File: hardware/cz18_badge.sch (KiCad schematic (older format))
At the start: 18 parts, among them U1 NRF24L01_Breakout

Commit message: Added 433MHz modules
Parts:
- RF1: footprint (none) -> Sensors:RF_Receiver_433_MHz
- RF2: footprint (none) -> Sensors:RF_Transmitter_433_MHz
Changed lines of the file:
@@
 LIBS:Zilog
 LIBS:skoro_sensors
-LIBS:cz18_badge-cache
 EELAYER 25 0
 EELAYER END
@@
 VCC
 $Comp
-L GNDREF #PWR2
+L GNDREF #PWR01
 U 1 1 5B016875
 P 1100 1400
-F 0 "#PWR2" H 1100 1150 50  0001 C CNN
+F 0 "#PWR01" H 1100 1150 50  0001 C CNN
 F 1 "GNDREF" H 1100 1250 50  0000 C CNN
 F 2 "" H 1100 1400 50  0001 C CNN
@@
 $EndComp
 $Comp
-L GNDREF #PWR6
+L GNDREF #PWR02
 U 1 1 5B016893
 P 2000 1400
-F 0 "#PWR6" H 2000 1150 50  0001 C CNN
+F 0 "#PWR02" H 2000 1150 50  0001 C CNN
 F 1 "GNDREF" H 2000 1250 50  0000 C CNN
 F 2 "" H 2000 1400 50  0001 C CNN
@@
 $EndComp
 $Comp
-L GNDREF #PWR8
+L GNDREF #PWR03
 U 1 1 5B016988
 P 2900 1400
-F 0 "#PWR8" H 2900 1150 50  0001 C CNN
+F 0 "#PWR03" H 2900 1150 50  0001 C CNN
 F 1 "GNDREF" H 2900 1250 50  0000 C CNN
 F 2 "" H 2900 1400 50  0001 C CNN
@@
 $EndComp
 $Comp
-L GNDREF #PWR10
+L GNDREF #PWR04
 U 1 1 5B016A28
 P 3800 1400
-F 0 "#PWR10" H 3800 1150 50  0001 C CNN
+F 0 "#PWR04" H 3800 1150 50  0001 C CNN
 F 1 "GNDREF" H 3800 1250 50  0000 C CNN
 F 2 "" H 3800 1400 50  0001 C CNN
@@
 $EndComp
 $Comp
-L GNDREF #PWR12
+L GNDREF #PWR05
 U 1 1 5B016A4B
 P 4750 1400
-F 0 "#PWR12" H 4750 1150 50  0001 C CNN
+F 0 "#PWR05" H 4750 1150 50  0001 C CNN
 F 1 "GNDREF" H 4750 1250 50  0000 C CNN
 F 2 "" H 4750 1400 50  0001 C CNN
@@
 $EndComp
 $Comp
-L GNDREF #PWR5
+L GNDREF #PWR06
 U 1 1 5B0170CF
 P 1600 750
-F 0 "#PWR5" H 1600 500 50  0001 C CNN
+F 0 "#PWR06" H 1600 500 50  0001 C CNN
 F 1 "GNDREF" H 1600 600 50  0000 C CNN
 F 2 "" H 1600 750 50  0001 C CNN
@@
 $EndComp
 $Comp
-L GNDREF #PWR1
+L GNDREF #PWR07
 U 1 1 5B0175AF
 P 700 750
-F 0 "#PWR1" H 700 500 50  0001 C CNN
+F 0 "#PWR07" H 700 500 50  0001 C CNN
 F 1 "GNDREF" H 700 600 50  0000 C CNN
 F 2 "" H 700 750 50  0001 C CNN
@@
 $EndComp
 $Comp
-L GNDREF #PWR7
+L GNDREF #PWR08
 U 1 1 5B0179B3
 P 2500 750
-F 0 "#PWR7" H 2500 500 50  0001 C CNN
+F 0 "#PWR08" H 2500 500 50  0001 C CNN
 F 1 "GNDREF" H 2500 600 50  0000 C CNN
 F 2 "" H 2500 750 50  0001 C CNN
@@
 $EndComp
 $Comp
-L GNDREF #PWR9
+L GNDREF #PWR09
 U 1 1 5B017A92
 P 3400 750
-F 0 "#PWR9" H 3400 500 50  0001 C CNN
+F 0 "#PWR09" H 3400 500 50  0001 C CNN
 F 1 "GNDREF" H 3400 600 50  0000 C CNN
 F 2 "" H 3400 750 50  0001 C CNN
@@
 $EndComp
 $Comp
-L GNDREF #PWR11
+L GNDREF #PWR010
 U 1 1 5B017AE5
 P 4350 750
-F 0 "#PWR11" H 4350 500 50  0001 C CNN
+F 0 "#PWR010" H 4350 500 50  0001 C CNN
 F 1 "GNDREF" H 4350 600 50  0000 C CNN
 F 2 "" H 4350 750 50  0001 C CNN
@@
 $EndComp
 $Comp
-L GNDREF #PWR14
+L GNDREF #PWR011
 U 1 1 5B01D44A
 P 9450 6150
-F 0 "#PWR14" H 9450 5900 50  0001 C CNN
+F 0 "#PWR011" H 9450 5900 50  0001 C CNN
 F 1 "GNDREF" H 9450 6000 50  0000 C CNN
 F 2 "" H 9450 6150 50  0001 C CNN
@@
 $EndComp
 $Comp
-L GNDREF #PWR3
+L GNDREF #PWR012
 U 1 1 5B01DF4E
 P 1250 6250
-F 0 "#PWR3" H 1250 6000 50  0001 C CNN
+F 0 "#PWR012" H 1250 6000 50  0001 C CNN
 F 1 "GNDREF" H 1250 6100 50  0000 C CNN
 F 2 "" H 1250 6250 50  0001 C CNN
@@
 $EndComp
 $Comp
-L GNDREF #PWR4
+L GNDREF #PWR013
 U 1 1 5B01DFBD
 P 1250 6700
-F 0 "#PWR4" H 1250 6450 50  0001 C CNN
+F 0 "#PWR013" H 1250 6450 50  0001 C CNN
 F 1 "GNDREF" H 1250 6550 50  0000 C CNN
 F 2 "" H 1250 6700 50  0001 C CNN
@@
 Connection ~ 9450 3650
 $Comp
-L VCC #PWR15
+L VCC #PWR014
 U 1 1 5B01FFB2
 P 9500 3550
-F 0 "#PWR15" H 9500 3400 50  0001 C CNN
+F 0 "#PWR014" H 9500 3400 50  0001 C CNN
 F 1 "VCC" H 9500 3700 50  0000 C CNN
 F 2 "" H 9500 3550 50  0001 C CNN
@@
 $EndComp
 $Comp
-L GNDREF #PWR13
+L GNDREF #PWR015
 U 1 1 5B024896
 P 5950 7400
-F 0 "#PWR13" H 5950 7150 50  0001 C CNN
+F 0 "#PWR015" H 5950 7150 50  0001 C CNN
 F 1 "GNDREF" H 5950 7250 50  0000 C CNN
 F 2 "" H 5950 7400 50  0001 C CNN
@@
 F 0 "RF1" H 3850 6950 60  0000 C CNN
 F 1 "RF_Receiver_433_MHz" H 3850 6850 60  0000 C CNN
-F 2 "" H 3950 6300 60  0000 C CNN
+F 2 "Sensors:RF_Receiver_433_MHz" H 3950 6300 60  0001 C CNN
 F 3 "" H 3950 6300 60  0000 C CNN
 	1    3850 6300
@@
 F 0 "RF2" H 3850 7950 60  0000 C CNN
 F 1 "RF_Transmitter_433_MHz" H 3850 7850 60  0000 C CNN
-F 2 "" H 3850 7150 60  0000 C CNN
+F 2 "Sensors:RF_Transmitter_433_MHz" H 3850 7150 60  0001 C CNN
 F 3 "" H 3850 7150 60  0000 C CNN
 	1    3850 7150

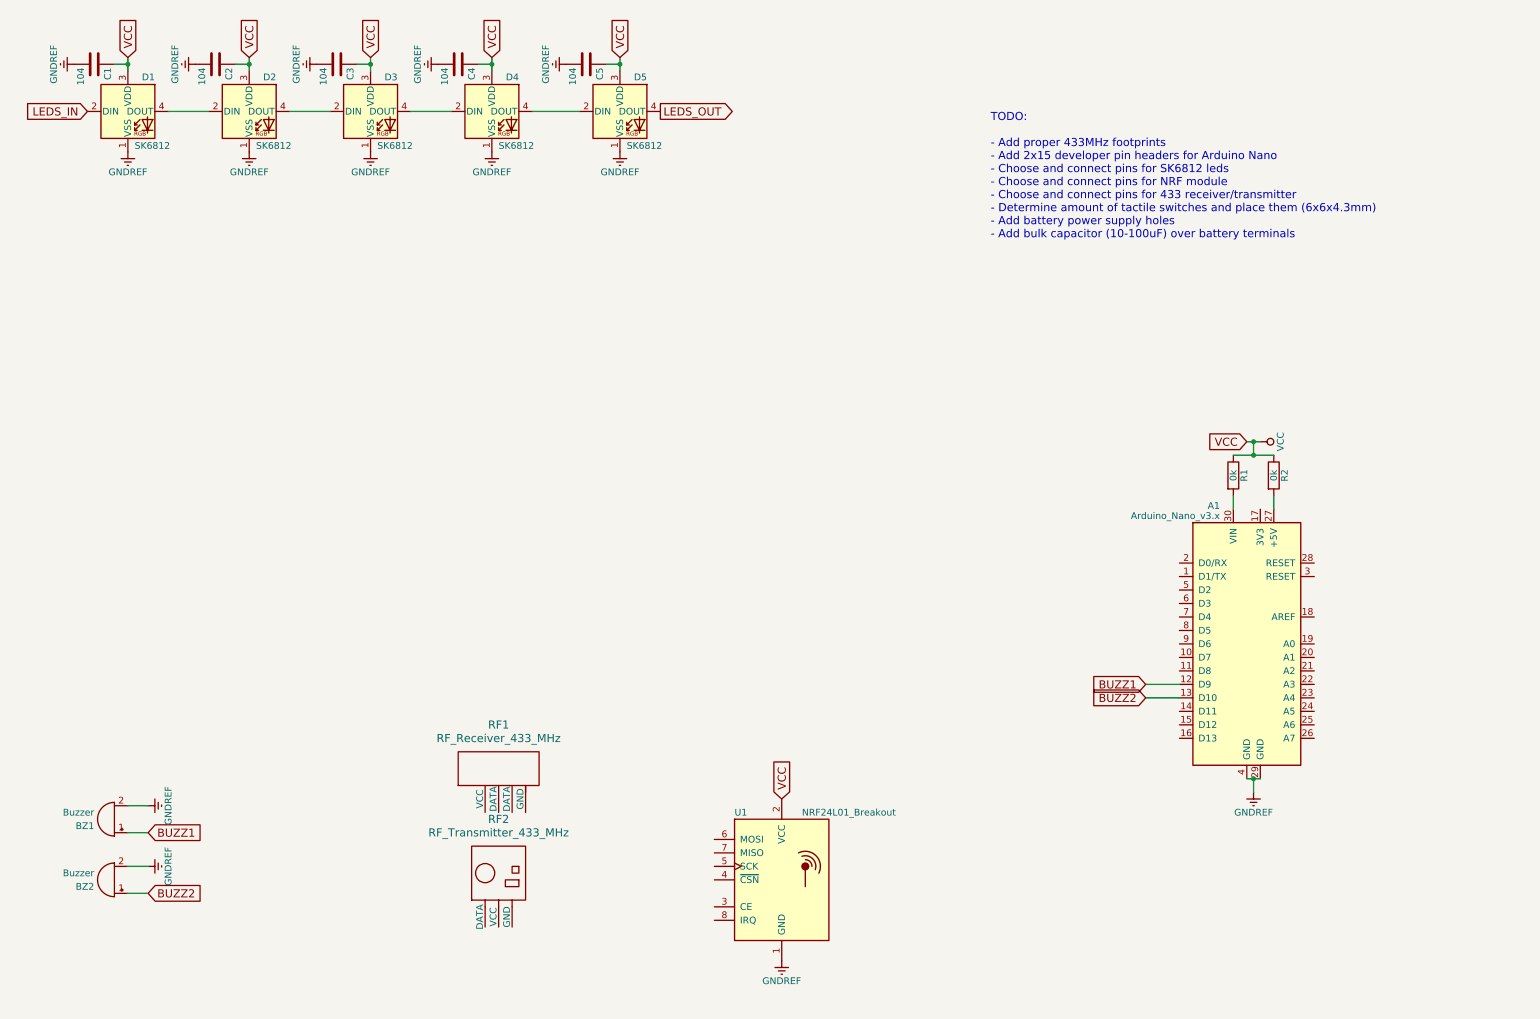
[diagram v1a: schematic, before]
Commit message: Connected component labels
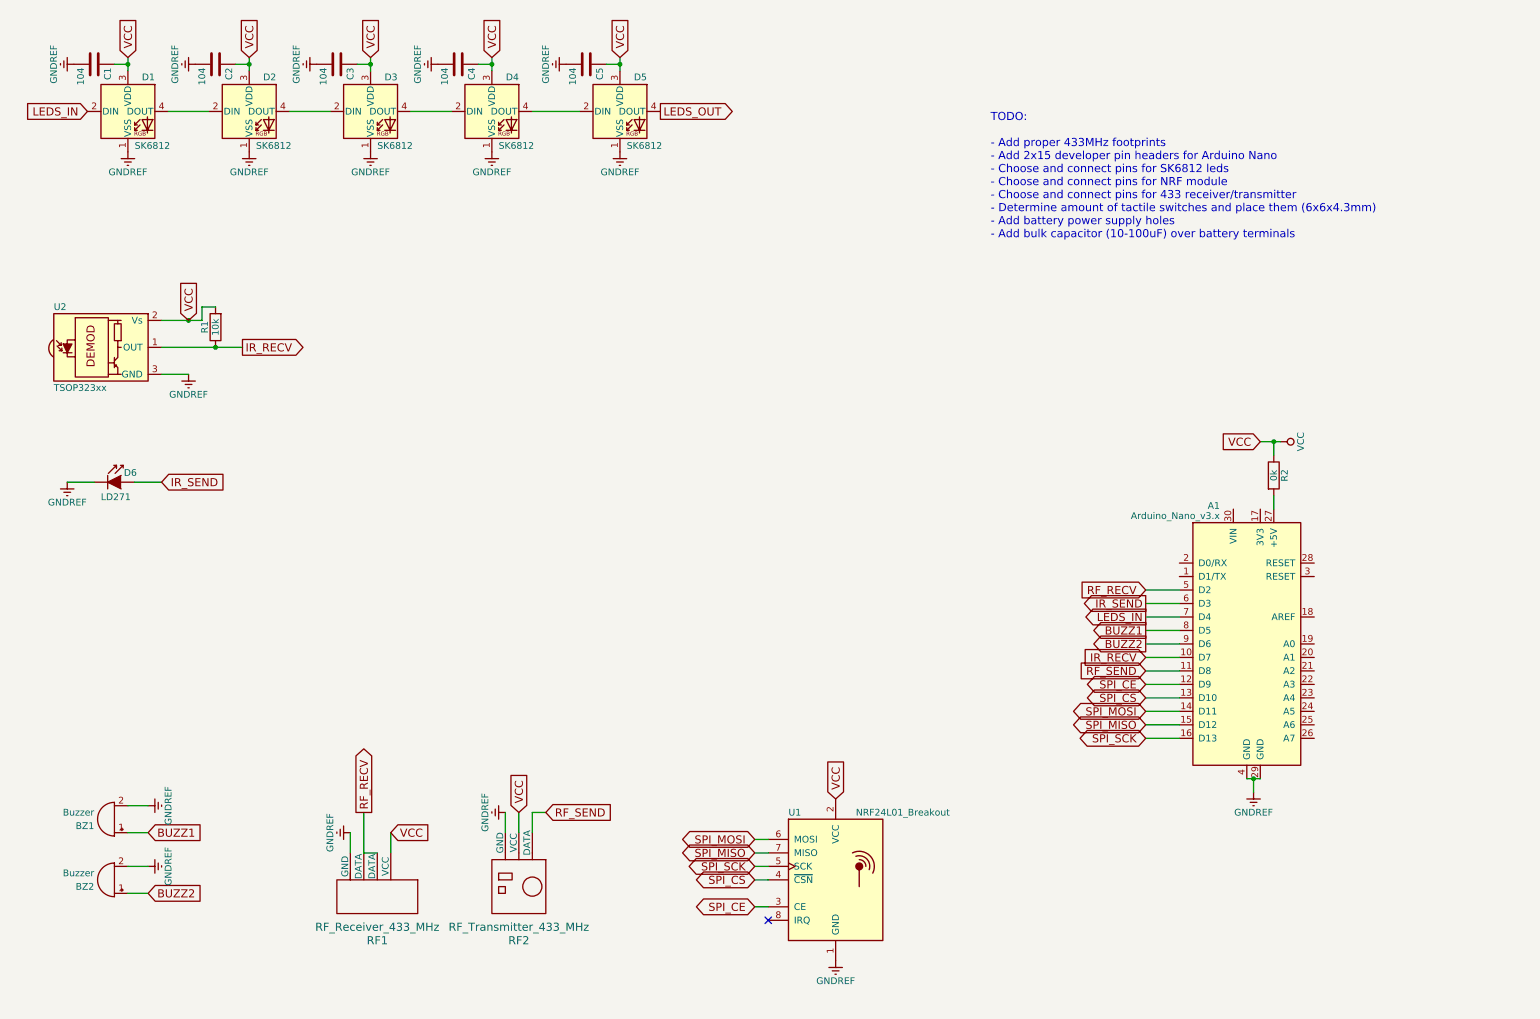
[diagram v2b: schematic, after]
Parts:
- added D6: LD271, LEDs:LED_D5.0mm, symbol LD271
- added U2: TSOP323xx, Opto-Devices:IRReceiver_Vishay_MOLD-3pin, symbol TSOP323xx
- R1: value 0k -> 10k
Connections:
- net BUZZ1: now also A1.8 (D5); no longer A1.12 (D9)
- net BUZZ2: now also A1.9 (D6); no longer A1.13 (D10)
- net GNDREF: now also RF1.4 (GND), RF2.3 (GND), D6.1 (K), U2.3 (GND)
- net LEDS_IN: now also A1.7 (D4)
- net VCC: now also R1.2, RF1.1 (VCC), RF2.2 (VCC), U2.2 (Vs); no longer R1.1
- net IR_RECV: now reaches A1.10 (D7)
- net IR_RECV: now also R1.1, U2.1 (OUT)
- net RF_SEND: now reaches A1.11 (D8)
- net RF_SEND: now also RF2.1 (DATA)
- net SPI_MOSI: now reaches A1.14 (D11)
- net SPI_MOSI: now also U1.6 (MOSI)
- net SPI_MISO: now reaches A1.15 (D12)
- net SPI_MISO: now also U1.7 (MISO)
- net SPI_SCK: now reaches A1.16 (D13)
- net SPI_SCK: now also U1.5 (SCK)
- net at A1.30 (VIN): no longer R1.2
- net RF_RECV: now reaches A1.5 (D2)
- net RF_RECV: now also RF1.2 (DATA), RF1.3 (DATA)
- net IR_SEND: now reaches A1.6 (D3)
- net IR_SEND: now also D6.2 (A)
- net SPI_CE: now reaches U1.3 (CE)
- net SPI_CE: now also A1.12 (D9)
- net SPI_CS: now reaches U1.4 (~CSN)
- net SPI_CS: now also A1.13 (D10)
- no-connect marks 0 -> 1
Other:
- moved on the sheet: RF1, RF2, U1

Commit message: Added battery and dev breakout, routed dev traces on test PCB
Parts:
- removed R2: 0k, Resistors_SMD:R_0603_HandSoldering, symbol R
- added BT1: Battery, Battery_Holders:Keystone_2479_3xAAA, symbol Battery
- added J1: Dev breakout, Pin_Headers:Pin_Header_Straight_2x15_Pitch2.54mm, symbol Conn_02x15_Odd_Even
- D6: value LD271 -> 940nm
- RF1: value RF_Receiver_433_MHz -> 433MHz Receiver
- RF2: value RF_Transmitter_433_MHz -> 433MHz Transmitter
- U1: value NRF24L01_Breakout -> NRF24L01
- U2: value TSOP323xx -> CHQ1838
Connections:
- net labels added: 3V3, A0, A1, A2, A3, A4, A5, A6, A7, AREF, D10, D11, D12, D13, D2, D3, D4, D5, D6, D7, D8, D9, GND, NRF_CE, RESET, RX, SPI_SS, TX, VIN
- net labels removed: SPI_CE, SPI_CS
- wire segments 55 -> 66
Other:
- note added: "TODO:\n\n- Determine amount of tactile switches and place them (6x6x4.3mm)\n- Add bulk capacitor (10-100uF) over battery terminals"
- note removed: "TODO:\n\n- Add proper 433MHz footprints\n- Add 2x15 developer pin headers for Arduino Nano\n- Choose and connect pins for SK6812 leds\n- Choose and connect pins for NRF module\n- Choose and connect pins for 433 receiver/transmitter\n- Determine amount of tactile switches and place them (6x6x4.3mm)\n- Add battery power supply holes\n- Add bulk capacitor (10-100uF) over battery terminals"
- moved on the sheet: C1, C2, C3, C4, C5, D1, D2, D3, D4, D5, D6, R1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

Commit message: Added buttons and 2 additional LEDs
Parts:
- added C6, C7: 104, Capacitors_SMD:C_0603_HandSoldering, symbol C
- added D6, D7: SK6812, LED_SMD:LED_SK6812_PLCC4_5.0x5.0mm_P3.2mm, symbol SK6812
- added SW1, SW2, SW3, SW4: SW_Push, Buttons_Switches_THT:SW_PUSH_6mm_h4.3mm, symbol SW_Push
- renumbered D6 to D8, RF2 to RF1, RF1 to RF2, U2 to U1, U1 to U2
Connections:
- net labels added: BTN_LEARN, BTN_MODE, BTN_PLAY, BTN_SLOT
- wire segments 66 -> 76
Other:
- note added: "2.4GHz NRF"
- note added: "433MHz RF"
- note added: "Audio"
- note added: "Battery"
- note added: "Breakout headers"
- note added: "Buttons"
- note added: "Controller"
- note added: "Infrared"
- note added: "LEDs"
- note added: "TODO:\n\n- Add bulk capacitor (10-100uF) over battery terminals"
- note removed: "TODO:\n\n- Determine amount of tactile switches and place them (6x6x4.3mm)\n- Add bulk capacitor (10-100uF) over battery terminals"
- moved on the sheet: A1, BZ1, BZ2, J1, RF1, RF2, U2

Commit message: Added Defcon Shitty AddOn footprint to pcb
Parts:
- removed BT1: Battery, Battery_Holders:Keystone_2479_3xAAA, symbol Battery
- added C8: 100uf, Capacitors_THT:C_Disc_D5.0mm_W2.5mm_P5.00mm, symbol C
- added J2: VCC (max 5V), Pin_Headers:Pin_Header_Straight_1x01_Pitch2.54mm, symbol Conn_01x01
- added J3: GND, Pin_Headers:Pin_Header_Straight_1x01_Pitch2.54mm, symbol Conn_01x01
- added J4: LEDS OUT, Pin_Headers:Pin_Header_Straight_1x01_Pitch2.54mm, symbol Conn_01x01
- added X1: Badgelife_shitty_connector, ShittyAddOn:Badgelife-Shitty-2x2, symbol Badgelife_shitty_connector
- SW1: value SW_Push -> MODE
- SW2: value SW_Push -> SLOT
- SW3: value SW_Push -> LEARN
- SW4: value SW_Push -> PLAY
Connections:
- net labels added: I2C_SCL, I2C_SDA
- net labels removed: LEDS_OUT
- wire segments 76 -> 82
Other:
- note added: "Defcon Shitty AddOn"
- note added: "TODO:\n\n- Add test points"
- note removed: "TODO:\n\n- Add bulk capacitor (10-100uF) over battery terminals"
- moved on the sheet: BZ1, BZ2
